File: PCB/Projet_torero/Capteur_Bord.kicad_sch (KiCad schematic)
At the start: 3 parts

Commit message: changement pins STlink
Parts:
- renumbered QRD801 to QRD901, R803 to R901, R804 to R902
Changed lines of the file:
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@@
+					(unit 1)
+				)
+				(path "/04e1eb47-a2c4-462b-bef7-377d9515a2c0/15f7fbe2-20f5-4588-8b16-1e568ab2921c/c5199f9a-575e-4cc6-940a-8598f60e0e2f"
+					(reference "#PWR0101")
 					(unit 1)
 				)
@@
 		(on_board yes)
 		(dnp no)
-		(property "Reference" "R803"
+		(property "Reference" "R901"
 			(at 158.75 115.57 90)
 			(effects
@@
 		(dnp no)
 		(fields_autoplaced yes)
-		(property "Reference" "QRD801"
+		(property "Reference" "QRD901"
 			(at 173.99 102.2349 0)
 			(effects
@@
 		(dnp no)
 		(fields_autoplaced yes)
-		(property "Reference" "#PWR0805"
+		(property "Reference" "#PWR0901"
 			(at 163.83 90.17 0)
 			(effects
@@
 		(dnp no)
 		(fields_autoplaced yes)
-		(property "Reference" "#PWR0807"
+		(property "Reference" "#PWR0903"
 			(at 170.18 92.71 0)
 			(effects
@@
 		(dnp no)
 		(fields_autoplaced yes)
-		(property "Reference" "#PWR0808"
+		(property "Reference" "#PWR0904"
 			(at 170.18 115.57 0)
 			(effects
@@
 		(on_board yes)
 		(dnp no)
-		(property "Reference" "R804"
+		(property "Reference" "R902"
 			(at 174.752 90.932 90)
 			(effects

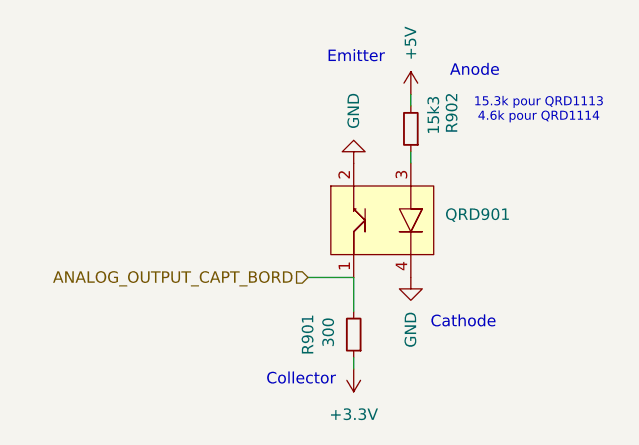
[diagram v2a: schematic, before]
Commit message: modif capteur de bord
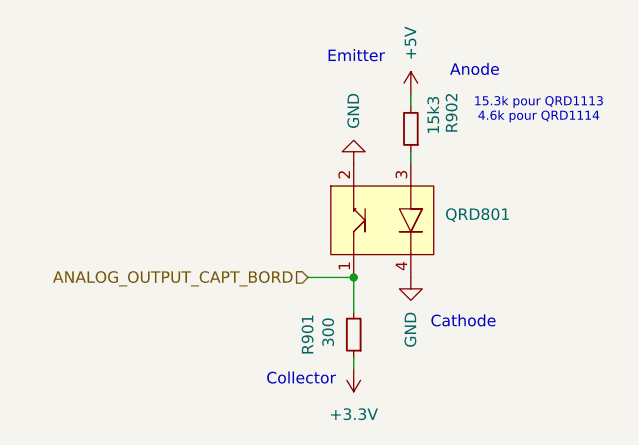
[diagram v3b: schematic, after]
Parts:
- removed QRD901: ~, Connector_JST:JST_EH_B4B-EH-A_1x04_P2.50mm_Vertical, symbol QRD1113:QRD1113
- added QRD801: ~, Connector_JST:JST_EH_B4B-EH-A_1x04_P2.50mm_Vertical, symbol QRD1113:QRD1113
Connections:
- net ANALOG_OUTPUT_CAPT_BORD: now also QRD801.1
- net GND: now also QRD801.2, QRD801.4
- net at R902.1: now also QRD801.3
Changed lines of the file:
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@@
 	(generator_version "8.0")
 	(paper "A4")
+	(junction
+		(at 163.83 109.22)
+		(diameter 0)
+		(color 0 0 0 0)
+	)
 	(wire
 		(pts
@@
 	)
 	(symbol
-		(lib_name "QRD1113_1")
 		(lib_id "QRD1113:QRD1113")
 		(at 179.07 102.87 0)
@@
 		(dnp no)
 		(fields_autoplaced yes)
-		(property "Reference" "QRD901"
+		(property "Reference" "QRD801"
 			(at 173.99 102.2349 0)
 			(effects
@@
 			)
 		)
+		(pin "1"
+		)
 		(pin "3"
 		)
@@
 		(pin "4"
 		)
-		(pin "1"
-		)
 		(instances

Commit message: maj pin STM
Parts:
- renumbered QRD801 to QRD901
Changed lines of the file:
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@@
 		(dnp no)
 		(fields_autoplaced yes)
-		(property "Reference" "QRD801"
+		(property "Reference" "QRD901"
 			(at 173.99 102.2349 0)
 			(effects

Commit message: modif placement composant
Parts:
- R901, R902: footprint (none) -> Resistor_SMD:R_0603_1608Metric
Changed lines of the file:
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@@
 			)
 		)
-		(property "Footprint" ""
+		(property "Footprint" "Resistor_SMD:R_0603_1608Metric"
 			(at 163.83 115.57 0)
 			(effects
@@
 			)
 		)
-		(property "Footprint" ""
+		(property "Footprint" "Resistor_SMD:R_0603_1608Metric"
 			(at 170.18 92.71 0)
 			(effects

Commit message: Placement des composants
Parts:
- QRD901: footprint Connector_JST:JST_EH_B4B-EH-A_1x04_P2.50mm_Vertical -> Connector_JST:JST_XH_S4B-XH-A_1x04_P2.50mm_Horizontal
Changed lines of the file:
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@@
 			)
 		)
-		(property "Footprint" "Connector_JST:JST_EH_B4B-EH-A_1x04_P2.50mm_Vertical"
+		(property "Footprint" "Connector_JST:JST_XH_S4B-XH-A_1x04_P2.50mm_Horizontal"
 			(at 179.07 102.87 0)
 			(effects

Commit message: Correction du PCB pour prof
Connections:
- net +5V is gone; now on net +3.3V: R902.2
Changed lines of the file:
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@@
 	)
 	(symbol
-		(lib_id "power:+5V")
+		(lib_id "power:+3.3V")
 		(at 170.18 88.9 0)
 		(unit 1)
@@
 		(dnp no)
 		(fields_autoplaced yes)
-		(property "Reference" "#PWR0903"
+		(property "Reference" "#PWR03"
 			(at 170.18 92.71 0)
 			(effects
@@
 			)
 		)
-		(property "Value" "+5V"
-			(at 170.1799 85.09 90)
+		(property "Value" "+3.3V"
+			(at 170.18 83.82 0)
 			(effects
 				(font
 					(size 1.27 1.27)
 				)
-				(justify left)
 			)
 		)
@@
 			)
 		)
-		(property "Description" "Power symbol creates a global label with name \"+5V\""
+		(property "Description" "Power symbol creates a global label with name \"+3.3V\""
 			(at 170.18 88.9 0)
 			(effects
@@
 		)
 		(instances
-			(project "Projet_torero"
+			(project ""
 				(path "/04e1eb47-a2c4-462b-bef7-377d9515a2c0/15f7fbe2-20f5-4588-8b16-1e568ab2921c/22646f91-6dfa-413c-9f84-f1d78dc63c5d"
-					(reference "#PWR0903")
+					(reference "#PWR04")
 					(unit 1)
 				)
 				(path "/04e1eb47-a2c4-462b-bef7-377d9515a2c0/15f7fbe2-20f5-4588-8b16-1e568ab2921c/c5199f9a-575e-4cc6-940a-8598f60e0e2f"
-					(reference "#PWR0803")
+					(reference "#PWR03")
 					(unit 1)
 				)
